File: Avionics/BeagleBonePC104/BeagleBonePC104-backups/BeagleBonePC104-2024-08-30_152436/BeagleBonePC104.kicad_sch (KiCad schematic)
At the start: 14 parts, among them U4 TJA1051T-3, U5 TMP36xS

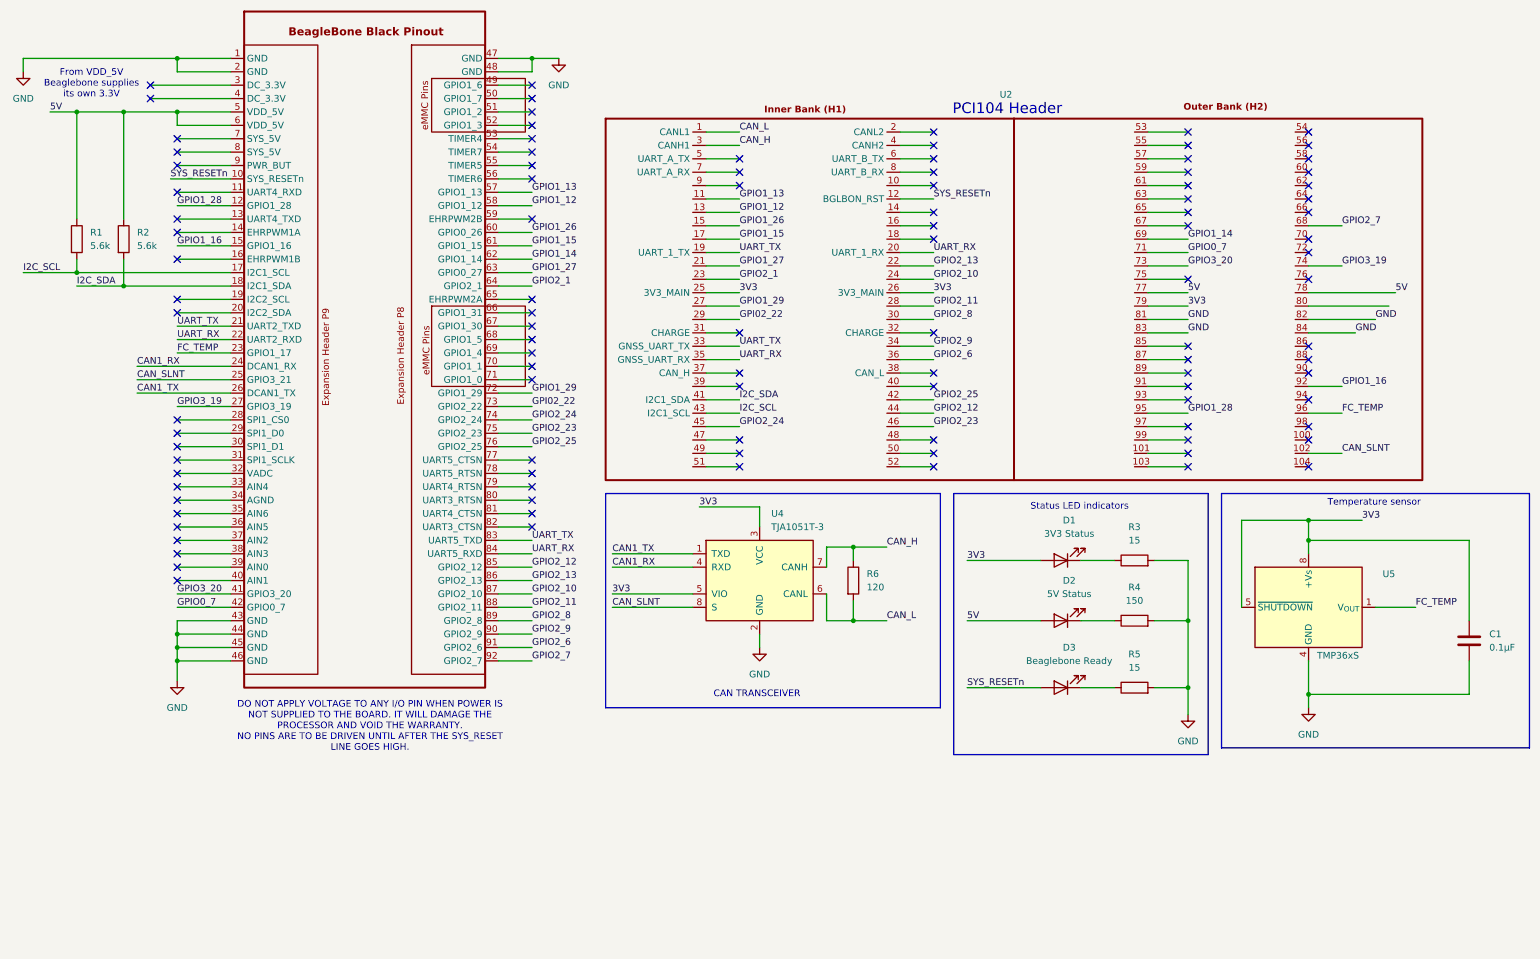
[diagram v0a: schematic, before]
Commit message: Ian Goldberg - Made changes to the third revision of the flight computer board, trying to figure out a way to power it throught ht header connector while still extracting data (through ethernet).
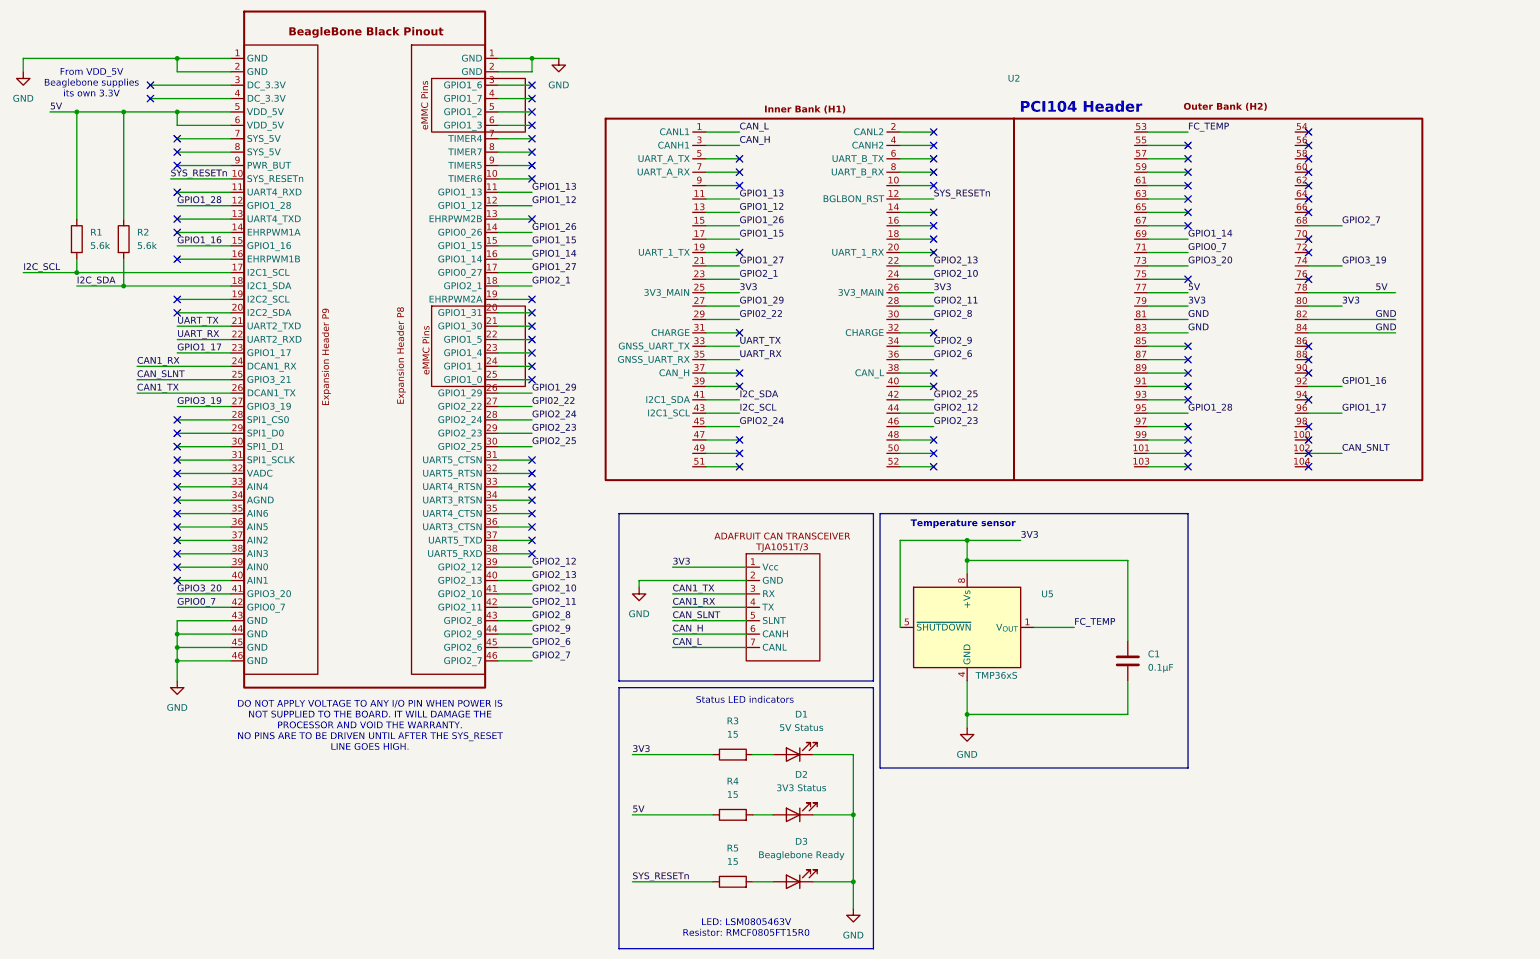
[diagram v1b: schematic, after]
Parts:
- removed R6: 120, Resistor_SMD:R_0805_2012Metric, symbol Device:R
- removed U4: TJA1051T-3, Package_SO:SOIC-8_3.9x4.9mm_P1.27mm, symbol Interface_CAN_LIN:TJA1051T-3
- added U3: ~, AdafruitCANTransciever:AdafruitCANPal_TJA1051T, symbol BeagleBoneBlackPinout:AdafruitCANTranscieverAttempt#2
- D1: value 3V3 Status -> 5V Status
- D2: value 5V Status -> 3V3 Status
- R3, R5: Wattage 1/8 -> (none)
- R4: value 150 -> 15; footprint Resistor_SMD:R_0603_1608Metric -> Resistor_SMD:R_0805_2012Metric; Wattage 1/16 -> (none)
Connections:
- net 3V3: now also R3.1, U2.80, U3.1 (Vcc); no longer D1.2 (A)
- net 5V: now also R4.1; no longer D2.2 (A)
- net CAN1_RX: now also U3.4 (TX)
- net CAN1_TX: now also U3.3 (RX)
- net CAN_H: now also U3.6 (CANH)
- net CAN_L: now also U3.7 (CANL)
- net CAN_SLNT: now also U3.5 (SLNT); no longer U2.102
- net FC_TEMP: now also U2.53; no longer U1.23 (GPIO1_17), U2.96
- net GND: now also D1.1 (K), D2.1 (K), D3.1 (K), U3.2 (GND); no longer R3.2, R4.2, R5.2, U1.47 (GND), U1.48 (GND)
- net GPI02_22: now also U1.27 (GPIO3_19); no longer U1.73 (GPIO2_22)
- net GPIO1_12: now also U1.12 (GPIO1_28); no longer U1.58 (GPIO1_12)
- net GPIO1_13: now also U1.11 (UART4_RXD); no longer U1.57 (GPIO1_13)
- net GPIO1_14: now also U1.16 (GPIO1_14); no longer U1.62 (GPIO1_14)
- net GPIO1_15: now also U1.15 (GPIO1_16); no longer U1.61 (GPIO1_15)
- net GPIO1_26: now also U1.14 (GPIO0_26); no longer U1.60 (GPIO0_26)
- net GPIO1_27: now also U1.17 (I2C1_SCL); no longer U1.63 (GPIO0_27)
- net GPIO1_29: now also U1.26 (GPIO1_29); no longer U1.72 (GPIO1_29)
- net GPIO2_1: now also U1.18 (I2C1_SDA); no longer U1.64 (GPIO2_1)
- net GPIO2_10: now also U1.41 (GPIO3_20); no longer U1.87 (GPIO2_10)
- net GPIO2_11: now also U1.42 (GPIO2_11); no longer U1.88 (GPIO2_11)
- net GPIO2_12: now also U1.39 (GPIO2_12); no longer U1.85 (GPIO2_12)
- net GPIO2_13: now also U1.40 (GPIO2_13); no longer U1.86 (GPIO2_13)
- net GPIO2_23: now also U1.29 (SPI1_D0); no longer U1.75 (GPIO2_23)
- net GPIO2_24: now also U1.28 (SPI1_CS0); no longer U1.74 (GPIO2_24)
- net GPIO2_25: now also U1.30 (SPI1_D1); no longer U1.76 (GPIO2_25)
- net GPIO2_6: now also U1.45 (GPIO2_6); no longer U1.91 (GPIO2_6)
- net GPIO2_7: now also U1.46 (GPIO2_7); no longer U1.92 (GPIO2_7)
- net GPIO2_8: now also U1.43 (GPIO2_8); no longer U1.89 (GPIO2_8)
- net GPIO2_9: now also U1.44 (GPIO2_9); no longer U1.90 (GPIO2_9)
- net SYS_RESETn: now also R5.1; no longer D3.2 (A)
- net UART_RX: no longer U1.84 (UART5_RXD), U2.20 (UART_1_RX)
- net UART_TX: no longer U1.83 (UART5_TXD), U2.19 (UART_1_TX)
- new net: D3.2 (A), R5.2
- new net: D1.2 (A), R3.2
- new net: D2.2 (A), R4.2
- new net CAN_SNLT: U2.102
- new net GPIO1_17: U1.23 (GPIO1_4), U2.96
- no-connect marks 104 -> 108
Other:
- note added: "LED: LSM0805463V Resistor: RMCF0805FT15R0"
- note removed: "CAN TRANSCEIVER"
- moved on the sheet: C1, D1, D2, D3, R3, R5, U5
